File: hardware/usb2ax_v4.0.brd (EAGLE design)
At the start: 22.5 x 15 mm, 37 parts, among them U1 IC_LPC11U14FET48/201, U2 IPC4282CZ6, U3 LD6805K/33P, U4 TPS71550DCKR or MIC5213-5.0YC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, U5 SN74AHC1G125DCKR, U6 SI8631EC-B-IS1, X1 CRYSTAL-306010047 12Mhz

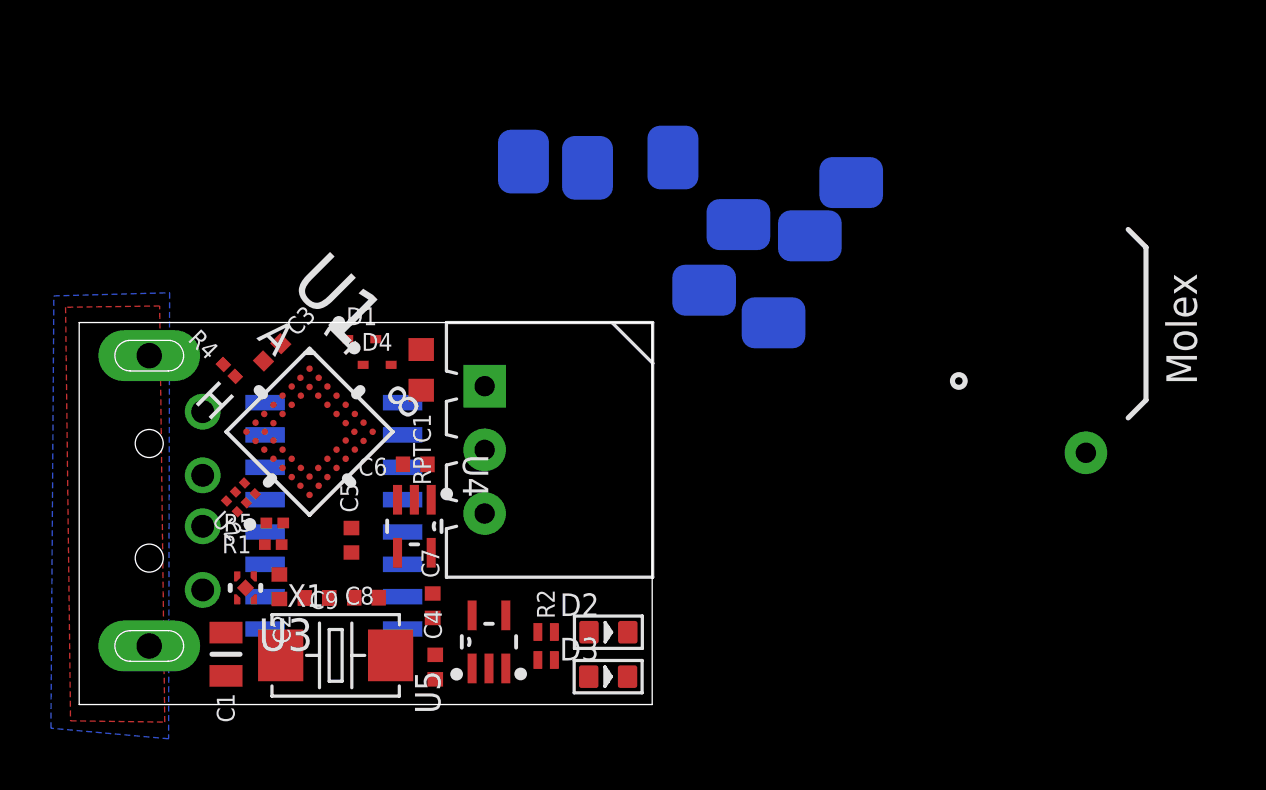
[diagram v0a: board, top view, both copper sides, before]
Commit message: v4 hardware: sch probably done, tentative routing.
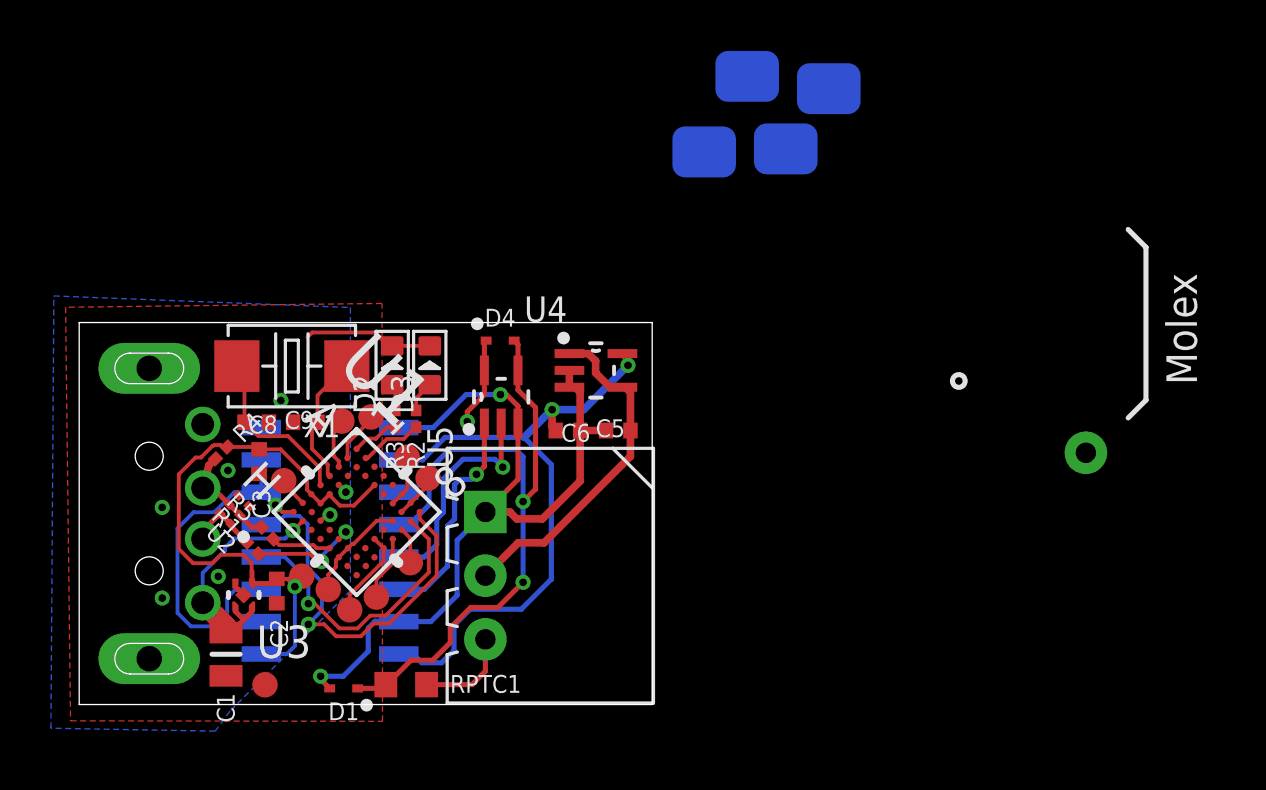
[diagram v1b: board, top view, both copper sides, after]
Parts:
- removed C4, C7: 1uF, Xevelabs:0402_N
- removed GND_SMD, HWB: PIN_SMD_2X2.5, Xevelabs:PIN_SMD_2X2.5
- added !TRST, +3.3V, SWCLK, SWDIO, TDI, TDO, TMS, TP1, TP2: PIN_SMD_1X1, Xevelabs:PIN_SMD_1X1
- added R3: 1k, Xevelabs:0201_N
- GND, RST: value PIN_SMD_2X2.5 -> PIN_SMD_1X1; device Xevelabs:PIN_SMD_2X2.5 -> Xevelabs:PIN_SMD_1X1
- R2: value 150R -> 1k; device Xevelabs:ARRAY_0402_65P_2_N -> Xevelabs:0201_N
- moved GND 23.9 mm to (7.29, 0.78), flipped to the top
- moved D3 14.1 mm to (13.8, 13.3), turned to 90 degrees
- moved D1 13.7 mm to (10.4, 0.64), turned to 180 degrees
- moved D2 13.5 mm to (12.3, 13.3), turned to 90 degrees
- moved RST 12.4 mm to (10.3, 11.1), flipped to the top, turned to 270 degrees
- moved RPTC1 12.4 mm to (12.8, 0.78), turned to 0 degrees
- moved X1 11.5 mm to (8.35, 13.3), turned to 180 degrees
- moved R2 10.3 mm to (13.2, 11.2), turned to 270 degrees
- moved U5 9.63 mm to (16.6, 12.1)
- moved C5 9.53 mm to (19.2, 10.8), turned to 0 degrees
- moved U4 9.40 mm to (20.3, 13.1), turned to 0 degrees
- moved C9 8.13 mm to (6.97, 11.1), turned to 0 degrees
- moved C6 8.08 mm to (21.2, 10.8)
- moved C8 6.92 mm to (8.88, 11.1), turned to 180 degrees
- moved SS 6.85 mm to (27.7, 21.8)
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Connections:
- removed net HWB: HWB.PIN
- removed net N$13: D2.+, R2.2
- removed net N$15: R2.3
- new net !TRST: !TRST.P$1, U1.A7, U1.B7
- new net LED_G: R2.2, U1.A2
- new net LED_R: R3.2, U1.A1
- new net N$1: TP1.P$1, U1.B1
- new net N$9: D2.+, R3.1
- new net SWCLK: SWCLK.P$1, U1.E7, U1.E8
- new net SWDIO: SWDIO.P$1, U1.A6, U1.B6
- new net TDI: TDI.P$1, U1.D8
- new net TDO: TDO.P$1, U1.C8
- new net TMS: TMS.P$1, U1.C7, U1.G6, U1.H6
- net +3V3: now also +3.3V.P$1, U1.F1, U1.F2; no longer C7.1
- net +5V: no longer C4.1
- net DIR_RX: now also U1.H1, U6.6
- net GND: now also GND.P$1, U1.G3; no longer C7.2, GND.PIN, GND_SMD.PIN
- net GNDIO: no longer C4.2
- net N$5: now also TP2.P$1, U1.G1; no longer R2.4
- net RST: now also RST.P$1; no longer RST.PIN
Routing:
- net GNDIO: track 0.00 -> 31.8 mm, vias 0 -> 2
- net +5V: track 0.00 -> 30.6 mm, vias 0 -> 3
- net N$4: track 0.00 -> 27.4 mm, vias 0 -> 2
- net +3V3: track 0.00 -> 23.6 mm, vias 0 -> 1
- net LPC_RX: track 0.00 -> 15.5 mm, vias 0 -> 1
- net DIR_RX: track 0.00 -> 14.5 mm, vias 0 -> 1
- net +12V: track 0.00 -> 13.4 mm
- net LPC_TX: track 0.00 -> 11.5 mm, vias 0 -> 1
- net VCC: track 0.00 -> 9.77 mm, vias 0 -> 1
- net N$3: track 0.00 -> 8.90 mm, vias 0 -> 1
- net N$24: track 0.00 -> 8.76 mm, vias 0 -> 1
- net N$7: track 0.00 -> 6.89 mm
- net GND: track 0.00 -> 6.57 mm, vias 0 -> 7
- net N$8: track 0.00 -> 5.26 mm
- net DM: track 0.00 -> 4.56 mm, vias 0 -> 2
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
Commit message: v4 hardware probably done.
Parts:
- removed MISO, MOSI, SCK, SS: PIN_SMD_2X2.5, Xevelabs:PIN_SMD_2X2.5
- removed RX: PIN_THT_0.8, Xevelabs:PIN_0.8
- moved U$1 13.8 mm to (1.90, 7.51), turned to 270 degrees
- moved GND 1.71 mm to (7.58, 2.46)
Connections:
- removed net N$17: MISO.PIN
- removed net N$18: MOSI.PIN
- removed net N$19: SCK.PIN
- removed net N$20: SS.PIN
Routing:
- net +5V: track 30.6 -> 29.4 mm
- net GNDIO: track 31.8 -> 31.2 mm
- net GND: vias 7 -> 8
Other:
- board text added: "+"
- board text added: "-"
- board text added: "D"
- board text added: "R"
- board text added: "T"
- board text added: "USB2MX-ISO"
- board text added: "en"
- board text added: "v1.0"
- board text removed: "(RX)"
- board text removed: "HWB"
- board text removed: "Molex"
- board text removed: "PB0"
- board text removed: "PB1"
- board text removed: "PB2"
- board text removed: "PB3"
- board text removed: "RST"
- board text removed: "USB2AX"
- board text removed: "v4.0a"
